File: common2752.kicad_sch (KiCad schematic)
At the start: 18 parts, among them U30 LTC2752B, U31 OPA2189DGK, U34 OPA2388DGK, U35 LTC2752B, U36 OPA2189DGK, U39 OPA2388DGK

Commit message: Adjust voltage rails.
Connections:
- net +18V renamed +19V
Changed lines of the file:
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@@
 	)
 	(symbol
-		(lib_id "Parts:+18V")
+		(lib_id "Parts:+19V")
 		(at 104.14 106.68 0)
 		(unit 1)
@@
 		(on_board yes)
 		(dnp no)
-		(property "Reference" "#PWR0345"
+		(property "Reference" "#PWR345"
 			(at 104.14 110.49 0)
 			(effects
@@
 			)
 		)
-		(property "Value" "+18V"
+		(property "Value" "+19V"
 			(at 104.14 103.124 0)
 			(do_not_autoplace yes)
@@
 			)
 		)
-		(property "Description" "Power symbol creates a global label with name {dblquote}+18V{dblquote}"
+		(property "Description" "Power symbol creates a global label with name \"+19\""
 			(at 104.14 106.68 0)
 			(effects
@@
 			(project "lincal"
 				(path "/b054cef4-39e3-49d8-aff0-7ba5a206c187/e42fba19-ca85-4742-a019-f67d1b8fc682"
-					(reference "#PWR0345")
+					(reference "#PWR345")
 					(unit 1)
 				)
@@
 	)
 	(symbol
-		(lib_id "Parts:+18V")
+		(lib_id "Parts:+19V")
 		(at 104.14 60.96 0)
 		(unit 1)
@@
 		(on_board yes)
 		(dnp no)
-		(property "Reference" "#PWR0255"
+		(property "Reference" "#PWR255"
 			(at 104.14 64.77 0)
 			(effects
@@
 			)
 		)
-		(property "Value" "+18V"
+		(property "Value" "+19V"
 			(at 104.14 57.404 0)
 			(do_not_autoplace yes)
@@
 			)
 		)
-		(property "Description" "Power symbol creates a global label with name {dblquote}+18V{dblquote}"
+		(property "Description" "Power symbol creates a global label with name \"+19\""
 			(at 104.14 60.96 0)
 			(effects
@@
 			(project "lincal"
 				(path "/b054cef4-39e3-49d8-aff0-7ba5a206c187/e42fba19-ca85-4742-a019-f67d1b8fc682"
-					(reference "#PWR0255")
+					(reference "#PWR255")
 					(unit 1)
 				)

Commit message: Progress checkin.  About to redo FDA feedback again.
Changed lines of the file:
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@@
 		(lib_id "Device:C")
 		(at 125.73 118.11 0)
-		(mirror y)
 		(unit 1)
 		(exclude_from_sim no)
@@
 					(size 1.27 1.27)
 				)
-				(justify left)
+				(justify right)
 			)
 		)
@@
 					(size 1.27 1.27)
 				)
-				(justify left)
+				(justify right)
 			)
 		)
 		(property "Footprint" "Capacitor_SMD:C_0402_1005Metric"
-			(at 124.7648 121.92 0)
+			(at 126.6952 121.92 0)
 			(effects
 				(font
@@
 		(lib_id "Device:C")
 		(at 125.73 110.49 0)
-		(mirror y)
 		(unit 1)
 		(exclude_from_sim no)
@@
 					(size 1.27 1.27)
 				)
-				(justify left)
+				(justify right)
 			)
 		)
@@
 					(size 1.27 1.27)
 				)
-				(justify left)
+				(justify right)
 			)
 		)
 		(property "Footprint" "Capacitor_SMD:C_0402_1005Metric"
-			(at 124.7648 114.3 0)
+			(at 126.6952 114.3 0)
 			(effects
 				(font
@@
 		(lib_id "Device:C")
 		(at 127 72.39 0)
-		(mirror y)
 		(unit 1)
 		(exclude_from_sim no)
@@
 					(size 1.27 1.27)
 				)
-				(justify left)
+				(justify right)
 			)
 		)
@@
 		)
 		(property "Footprint" "Capacitor_SMD:C_0402_1005Metric"
-			(at 126.0348 76.2 0)
+			(at 127.9652 76.2 0)
 			(effects
 				(font
@@
 		(lib_id "Device:C")
 		(at 127 64.77 0)
-		(mirror y)
 		(unit 1)
 		(exclude_from_sim no)
@@
 					(size 1.27 1.27)
 				)
-				(justify left)
+				(justify right)
 			)
 		)
@@
 					(size 1.27 1.27)
 				)
-				(justify left)
+				(justify right)
 			)
 		)
 		(property "Footprint" "Capacitor_SMD:C_0402_1005Metric"
-			(at 126.0348 68.58 0)
-			(effects
-				(font
+			(at 127.9652 68.58 0)
+			(effects
+				(font

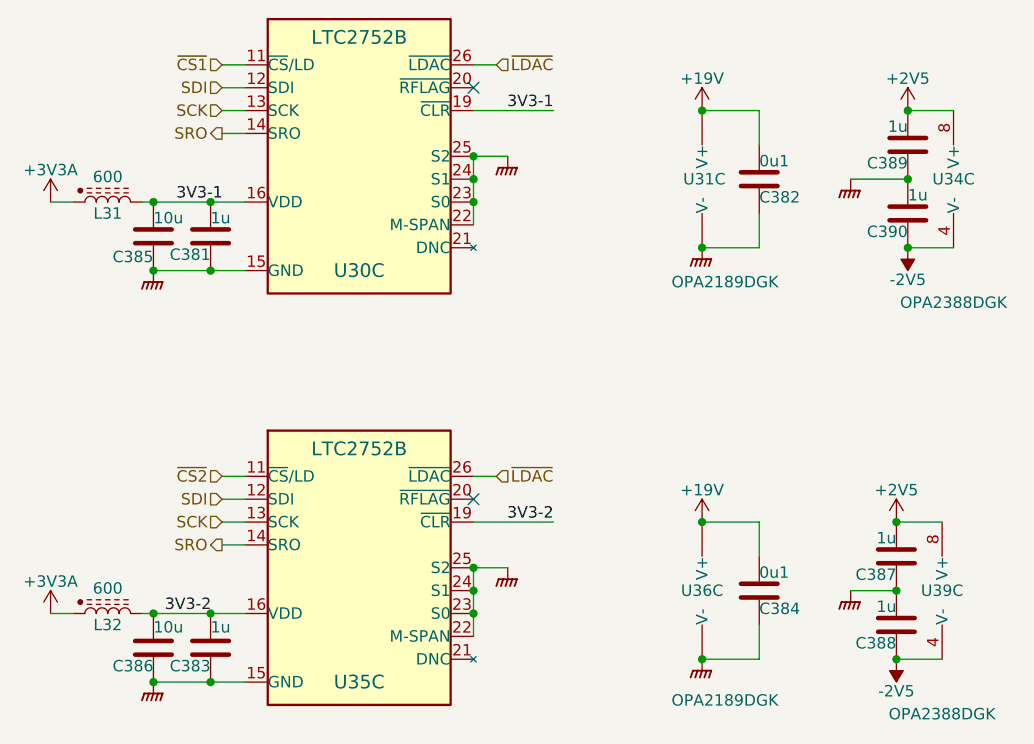
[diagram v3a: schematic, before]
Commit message: Start to place within physical board size.
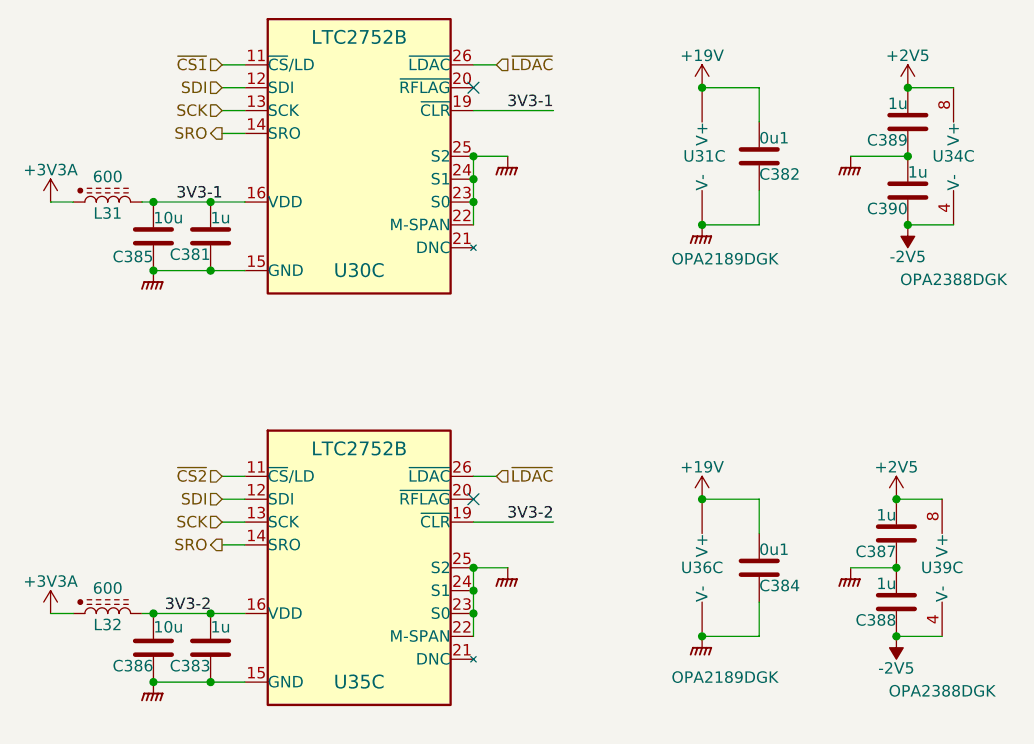
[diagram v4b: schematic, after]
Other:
- moved on the sheet: C382, C384, C387, C388, C389, C390, U31C, U34C, U36C, U39C

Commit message: Rationalise and more SPI tidy.
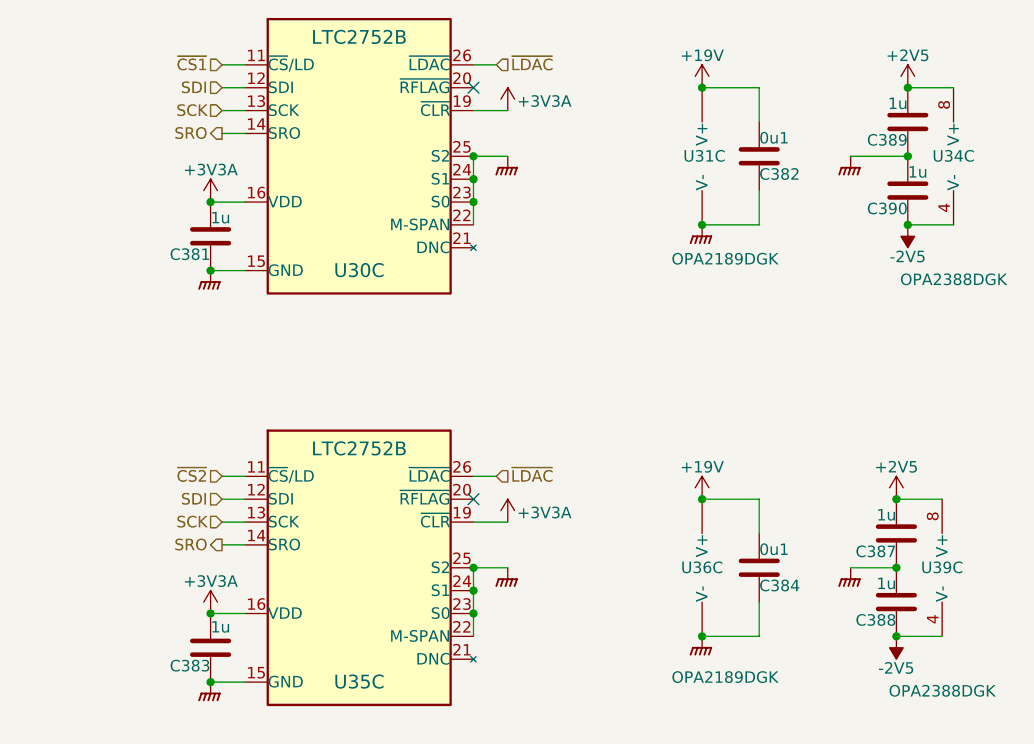
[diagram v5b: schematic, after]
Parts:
- removed C385, C386: 10u, Capacitor_SMD:C_0603_1608Metric, symbol Device:C
- removed L31, L32: 600, Inductor_SMD:L_0603_1608Metric, symbol Parts:L_Ferrite_Power
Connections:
- net 3V3-1 is gone; now on net +3V3A: C381.1, U30.16 (VDD), U30.19 (~{CLR})
- net 3V3-2 is gone; now on net +3V3A: C383.1, U35.16 (VDD), U35.19 (~{CLR})

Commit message: More component metadata.
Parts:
- C381, C382, C383, C384, C387, C388, C389, C390, U30, U35: Stock (none) -> JLC
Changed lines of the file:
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@@
 			)
 		)
-		(property "Stock" ""
+		(property "Stock" "JLC"
 			(at 125.73 115.57 0)
 			(effects
@@
 			)
 		)
-		(property "Stock" ""
+		(property "Stock" "JLC"
 			(at 66.04 66.04 0)
 			(effects
@@
 			)
 		)
-		(property "Stock" ""
+		(property "Stock" "JLC"
 			(at 110.49 111.76 0)
 			(effects
@@
 			)
 		)
-		(property "Stock" ""
+		(property "Stock" "JLC"
 			(at 66.04 111.76 0)
 			(effects
@@
 			)
 		)
-		(property "Stock" ""
+		(property "Stock" "JLC"
 			(at 125.73 107.95 0)
 			(effects
@@
 			)
 		)
-		(property "Stock" ""
+		(property "Stock" "JLC"
 			(at 110.49 66.04 0)
 			(effects
@@
 			)
 		)
-		(property "Stock" ""
+		(property "Stock" "JLC"
 			(at 49.53 74.93 0)
 			(effects
@@
 			)
 		)
-		(property "Stock" ""
+		(property "Stock" "JLC"
 			(at 127 69.85 0)
 			(effects
@@
 			)
 		)
-		(property "Stock" ""
+		(property "Stock" "JLC"
 			(at 49.53 120.65 0)
 			(effects
@@
 			)
 		)
-		(property "Stock" ""
+		(property "Stock" "JLC"
 			(at 127 62.23 0)
 			(effects

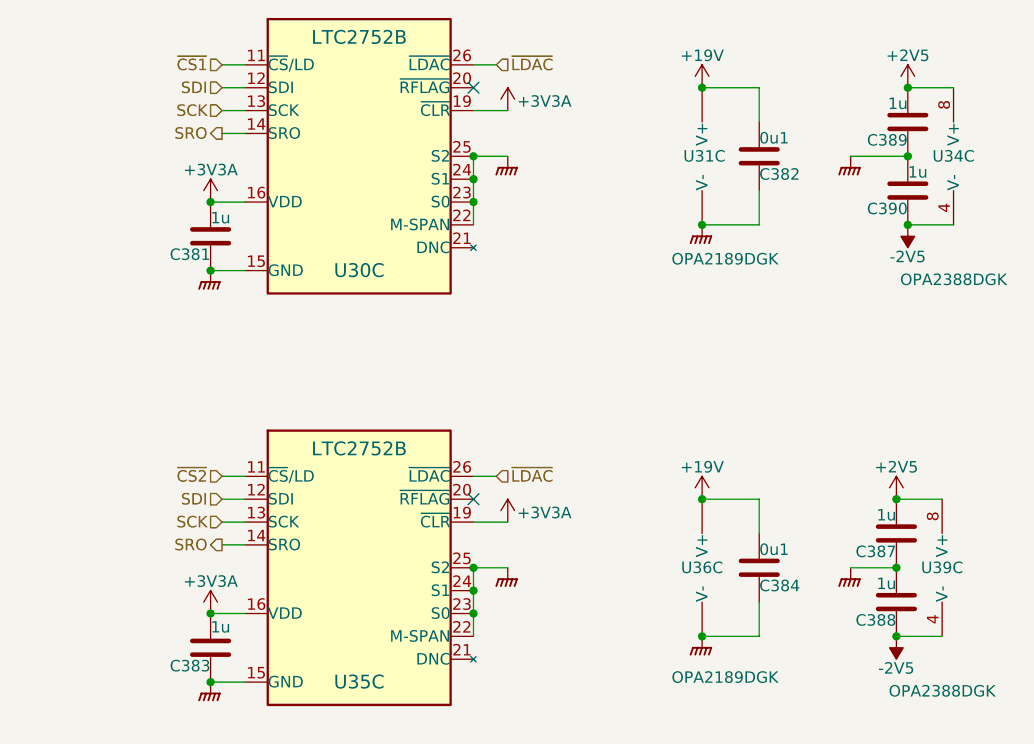
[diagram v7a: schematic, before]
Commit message: Change some footprints.
Mounting holes for covers.
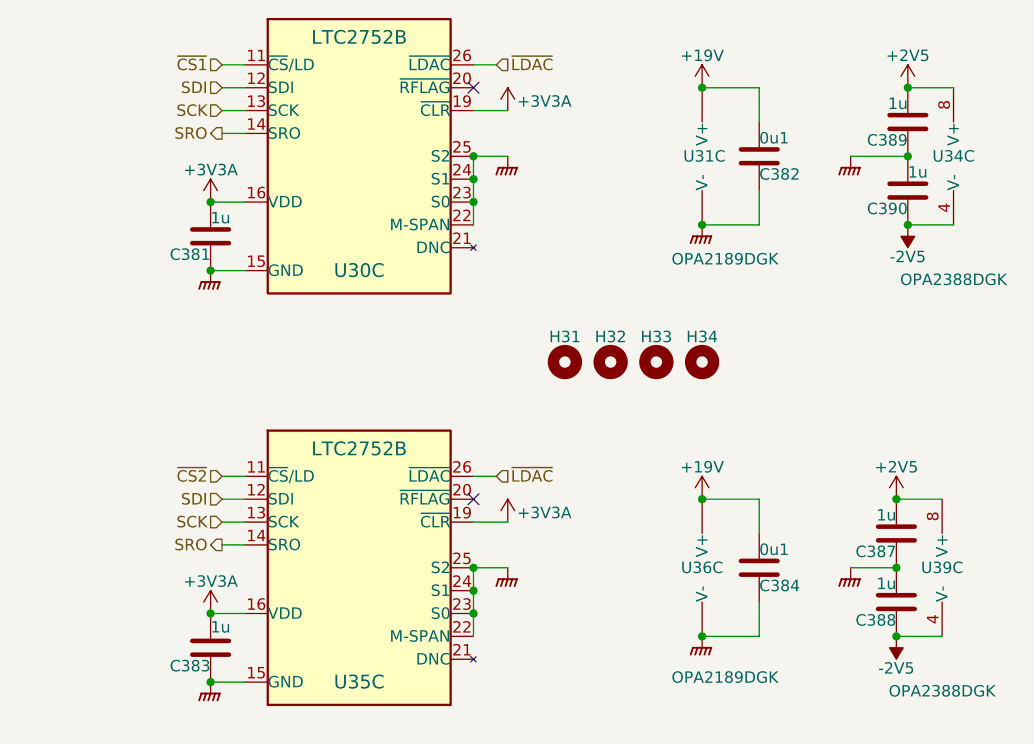
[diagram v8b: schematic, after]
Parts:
- added H31, H32, H33, H34: MountingHole, Parts:Hole_1.5mm_Unplated, symbol Mechanical:MountingHole
